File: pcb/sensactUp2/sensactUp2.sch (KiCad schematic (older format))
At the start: 38 parts, among them J1 PROG, J2 BUS, J3 EXT, J4 EXT_BUT, J5 BUS, J6 1Wire, Q3 Q_NPN_BEC, SW1 RotEnc, SW2 SW_Push, U1 ESP32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

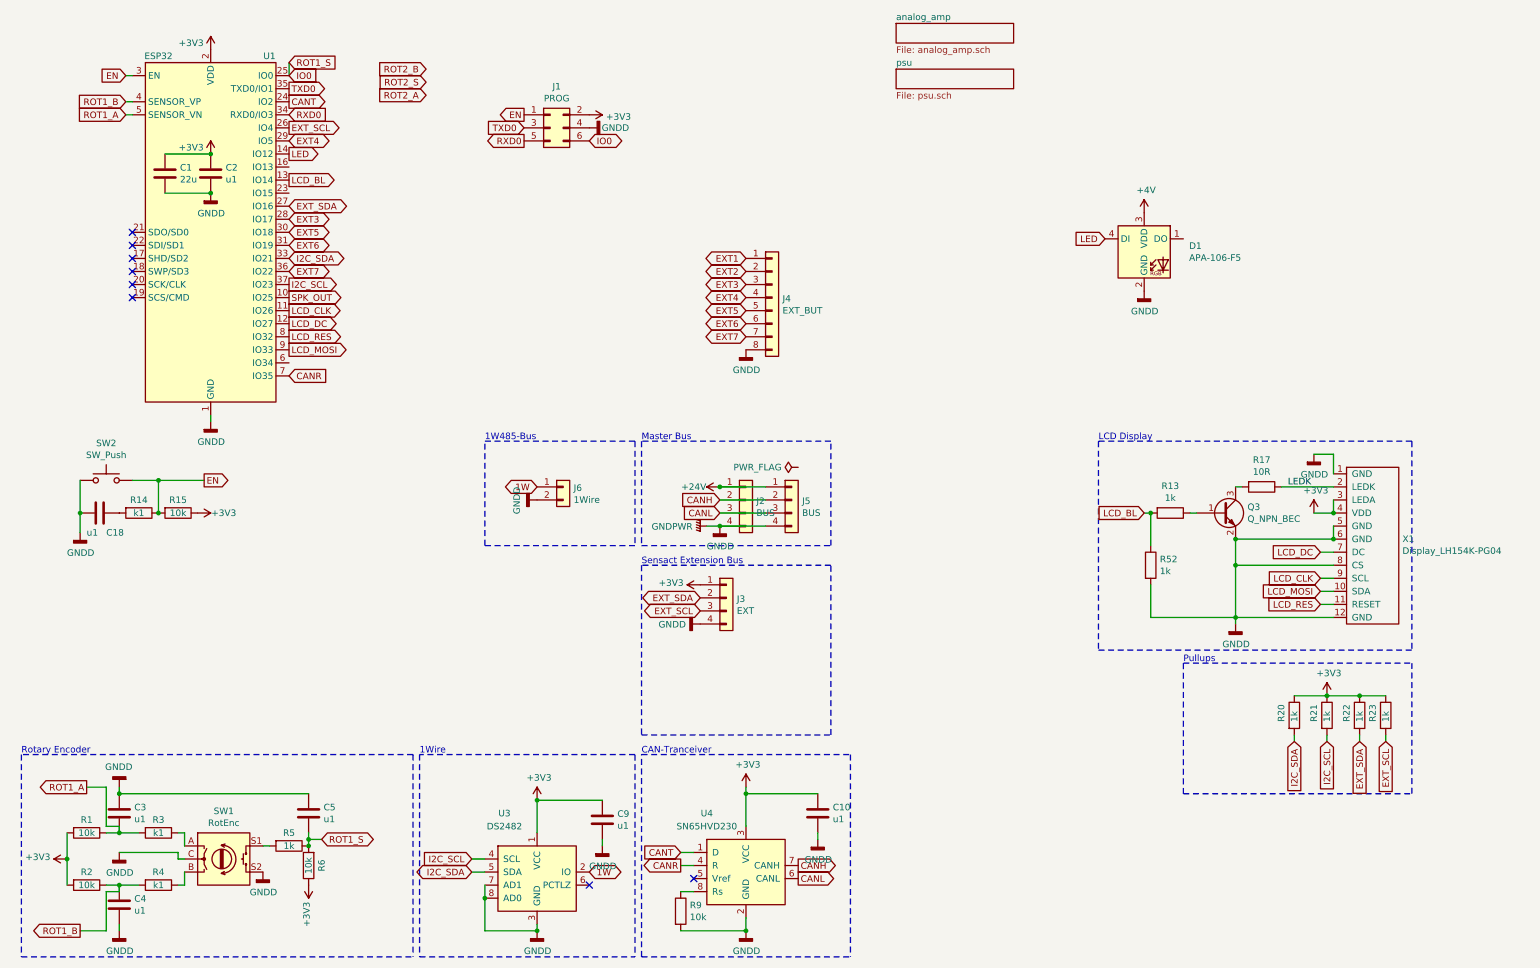
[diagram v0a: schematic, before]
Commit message: sensactUP2, sensactHsNano sensactHsLED sensactOutdoor as ordered at JLCPCB
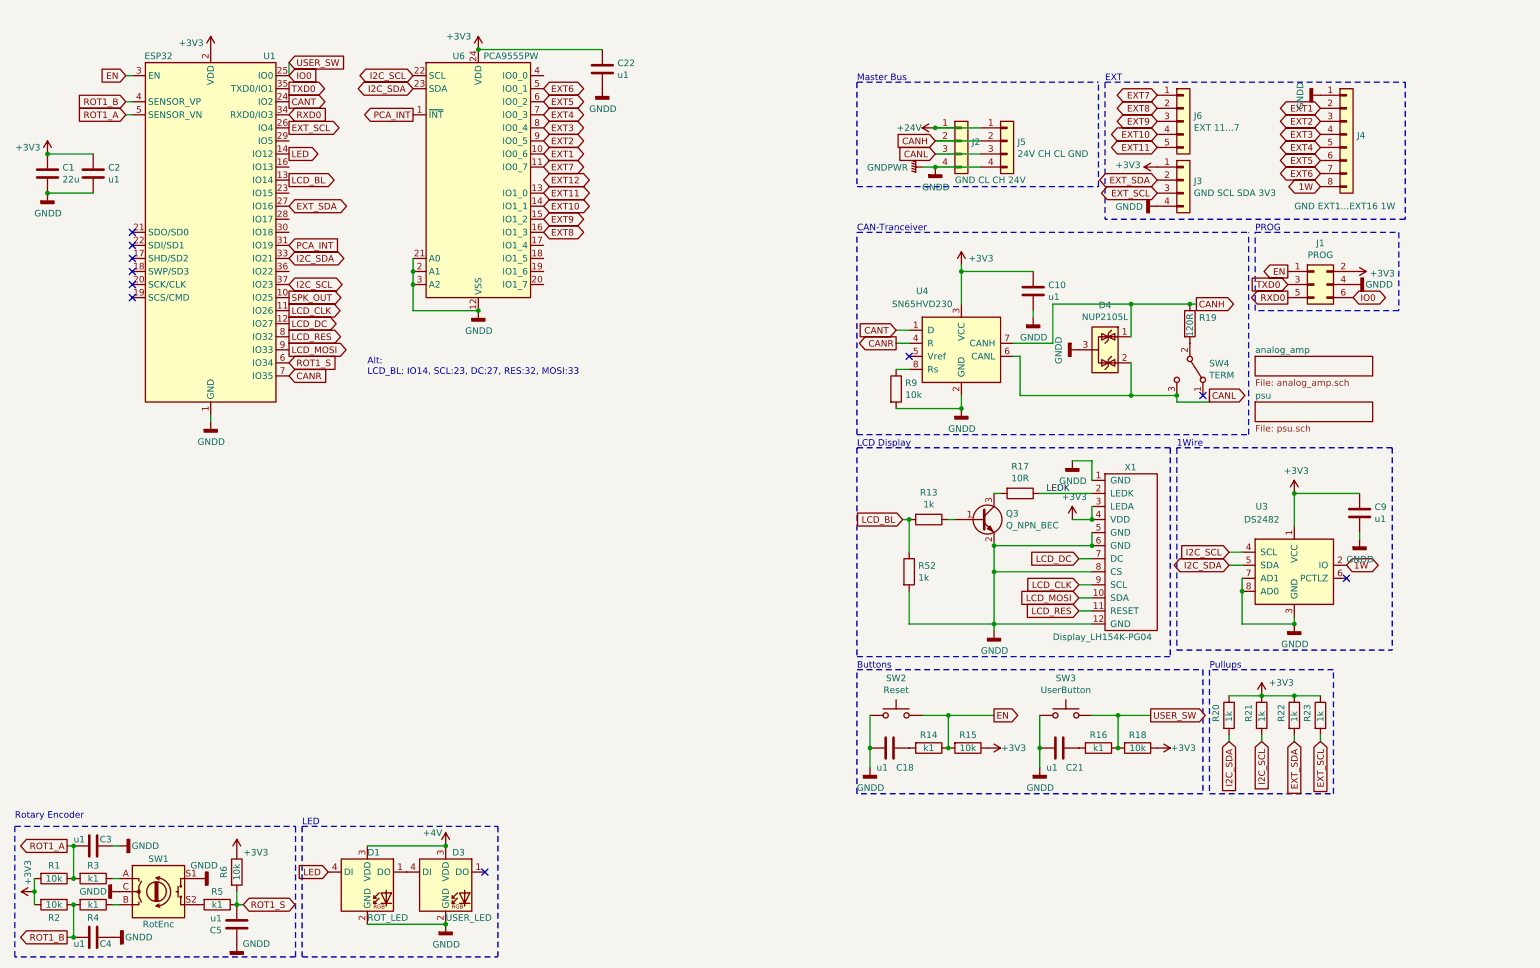
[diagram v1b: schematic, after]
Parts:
- removed J6: 1Wire, Connector_Phoenix_MC:PhoenixContact_MCV_1,5_2-G-3.5_1x02_P3.50mm_Vertical, symbol Connector_Generic:Conn_01x02
- added C21, C22: u1, Capacitor_SMD:C_0805_2012Metric_Pad1.18x1.45mm_HandSolder, symbol Device:C
- added D3: USER_LED, LED_THT:LED_D5.0mm-4_RGB, symbol LED:APA-106-F5
- added D4: NUP2105L, Package_TO_SOT_SMD:SOT-23_Handsoldering, symbol Power_Protection:NUP2105L
- added J6: EXT 11...7, Connector_PinHeader_2.54mm:PinHeader_1x05_P2.54mm_Vertical, symbol Connector_Generic:Conn_01x05
- added R16: k1, Resistor_SMD:R_0805_2012Metric_Pad1.20x1.40mm_HandSolder, symbol Device:R
- added R18: 10k, Resistor_SMD:R_0805_2012Metric_Pad1.20x1.40mm_HandSolder, symbol Device:R
- added R19: 120R, Resistor_SMD:R_0805_2012Metric_Pad1.20x1.40mm_HandSolder, symbol Device:R
- added SW3: UserButton, Button_Switch_THT:SW_PUSH_6mm_H13mm, symbol Switch:SW_Push
- added SW4: TERM, liebler_MECH:SW_SPDT_PCM12_handsolder, symbol Switch:SW_SPDT
- added U6: PCA9555PW, liebler_SEMICONDUCTORS:TSSOP-24_4.4x7.8mm_Pitch0.65mm_handsolder, symbol Interface_Expansion:PCA9555PW
- D1: value APA-106-F5 -> ROT_LED
- J2: value BUS -> GND CL CH 24V
- J3: value EXT -> GND SCL SDA 3V3
- J4: value EXT_BUT -> GND EXT1...EXT16 1W; footprint Connector_Phoenix_MC:PhoenixContact_MCV_1,5_8-G-3.5_1x08_P3.50mm_Vertical -> liebler_CONN:PhoenixContact_MCV_0,5_8-G-2.5_1x08_P2.50mm_vertical
- J5: value BUS -> 24V CH CL GND
- R5: value 1k -> k1
- SW2: value SW_Push -> Reset
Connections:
- net +3V3: now also C22.1, R18.1, U6.24 (VDD)
- net +4V: now also D3.3 (VDD)
- net 1W: now also J4.8 (Pin_8)
- net CANH: now also D4.1 (K), R19.1
- net CANL: now also D4.2 (K), SW4.3 (C)
- net EXT1: now also J4.2 (Pin_2), U6.10 (IO0_6); no longer J4.1 (Pin_1)
- net EXT2: now also J4.3 (Pin_3), U6.9 (IO0_5); no longer J4.2 (Pin_2)
- net EXT3: now also J4.4 (Pin_4), U6.8 (IO0_4); no longer J4.3 (Pin_3), U1.28 (IO17)
- net EXT4: now also J4.5 (Pin_5), U6.7 (IO0_3); no longer J4.4 (Pin_4), U1.29 (IO5)
- net EXT5: now also J4.6 (Pin_6), U6.6 (IO0_2); no longer J4.5 (Pin_5), U1.30 (IO18)
- net EXT6: now also J4.7 (Pin_7), U6.5 (IO0_1); no longer J4.6 (Pin_6), U1.31 (IO19)
- net EXT7: now also J6.1 (Pin_1), U6.11 (IO0_7); no longer J4.7 (Pin_7), U1.36 (IO22)
- net GNDD: now also C4.1, J4.1 (Pin_1), SW1.S1, C21.2, C22.2, D3.2 (GND), D4.3 (A), SW3.2, U6.12 (VSS), U6.2 (A1), U6.21 (A0), U6.3 (A2); no longer C4.2, J4.8 (Pin_8), SW1.S2
- net I2C_SCL: now also U6.22 (SCL)
- net I2C_SDA: now also U6.23 (SDA)
- net IO0: now also R16.1, R18.2, SW3.1; no longer C5.2, R5.1, R6.2
- net ROT1_B: now also C4.2; no longer C4.1
- net ROT1_S: now reaches U1.6 (IO34)
- net ROT1_S: now also C5.2, R5.1, R6.2
- net at R5.2: now also SW1.S2; no longer SW1.S1
- net at D1.1 (DO): now also D3.4 (DI)
- new net: C21.1, R16.2
- new net: R19.2, SW4.2 (B)
- new net EXT10: J6.4 (Pin_4), U6.14 (IO1_1)
- new net EXT11: J6.5 (Pin_5), U6.13 (IO1_0)
- new net EXT8: J6.2 (Pin_2), U6.16 (IO1_3)
- new net EXT9: J6.3 (Pin_3), U6.15 (IO1_2)
- new net PCA_INT: U1.31 (IO19), U6.1 (~INT)
- no-connect marks 8 -> 10
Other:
- note added: "Alt:\nLCD_BL: IO14, SCL:23, DC:27, RES:32, MOSI:33"
- note added: "Buttons"
- note added: "EXT"
- note added: "LED"
- note added: "PROG"
- note removed: "1W485-Bus"
- note removed: "Sensact Extension Bus"
- moved on the sheet: C1, C10, C18, C2, C3, C4, C5, C9, D1, J1, J2, J3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

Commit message: sensactHsNano for Reflow Soldering
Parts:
- D1, D3: footprint LED_THT:LED_D5.0mm-4_RGB -> LED_THT:LED_D5.0mm-4_RGB_Staggered_Pins
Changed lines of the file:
@@
 F 0 "D1" H 3200 7450 50  0000 L CNN
 F 1 "ROT_LED" H 3200 6950 50  0000 L CNN
-F 2 "LED_THT:LED_D5.0mm-4_RGB" H 3250 6900 50  0001 L TNN
+F 2 "LED_THT:LED_D5.0mm-4_RGB_Staggered_Pins" H 3250 6900 50  0001 L TNN
 F 3 "https://cdn.sparkfun.com/datasheets/Components/LED/COM-12877.pdf" H 3300 6825 50  0001 L TNN
 	1    3200 7200
@@
 F 0 "D3" H 3850 7450 50  0000 L CNN
 F 1 "USER_LED" H 3800 6950 50  0000 L CNN
-F 2 "LED_THT:LED_D5.0mm-4_RGB" H 3850 6900 50  0001 L TNN
+F 2 "LED_THT:LED_D5.0mm-4_RGB_Staggered_Pins" H 3850 6900 50  0001 L TNN
 F 3 "https://cdn.sparkfun.com/datasheets/Components/LED/COM-12877.pdf" H 3900 6825 50  0001 L TNN
 	1    3800 7200
@@
 Connection ~ 750  1600
 $Comp
-L power:GNDD #PWR?
+L power:GNDD #PWR012
 U 1 1 610E1F2E
 P 2200 7650
-F 0 "#PWR?" H 2200 7400 50  0001 C CNN
+F 0 "#PWR012" H 2200 7400 50  0001 C CNN
 F 1 "GNDD" H 2350 7650 50  0000 C CNN
 F 2 "" H 2200 7650 50  0001 C CNN
